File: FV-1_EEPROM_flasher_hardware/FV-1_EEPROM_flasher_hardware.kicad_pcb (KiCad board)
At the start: 2 copper layers, 64.9 x 84.9 mm, 20 parts, among them J1 TFT_SD, SW1 Up, SW2 Down, SW3 Right, SW4 Left, SW5 select, U1 24LC32, U2 24LC32

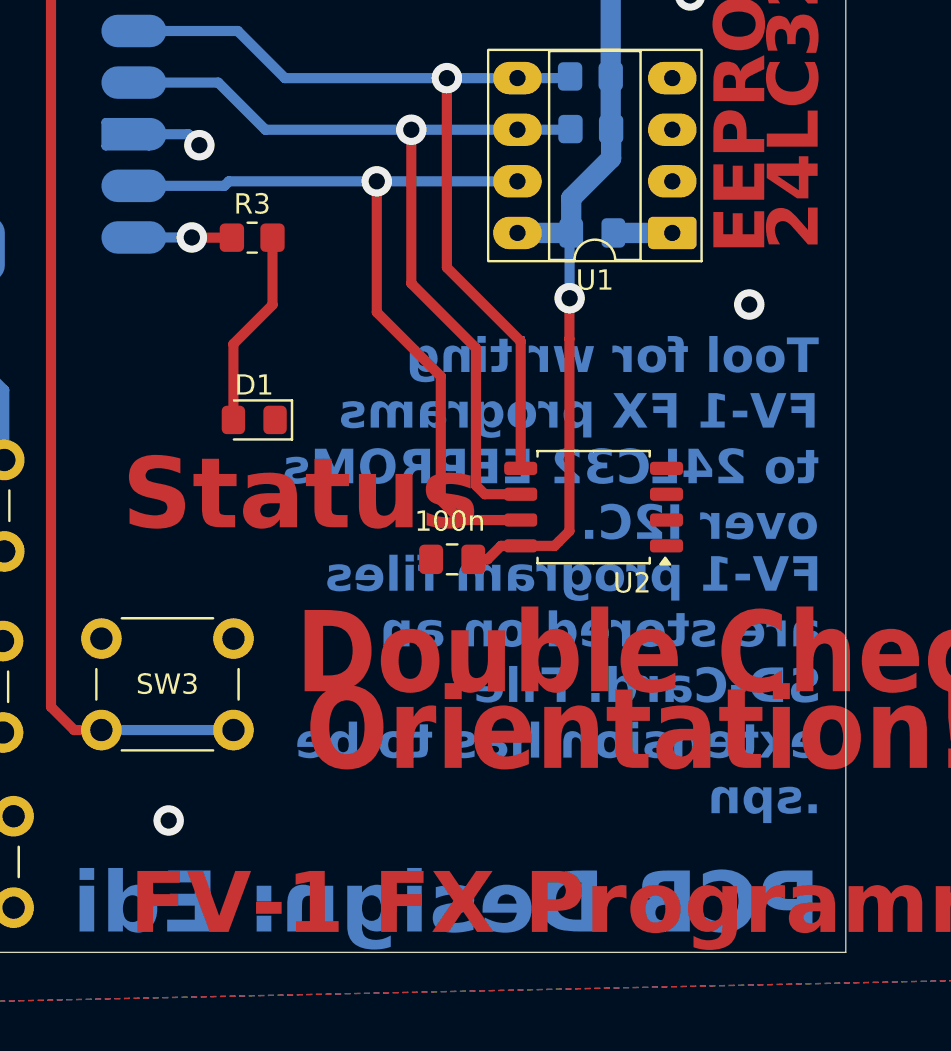
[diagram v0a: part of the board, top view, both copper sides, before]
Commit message: replaced status led with shift button, led connected to EEPROM write protect pin
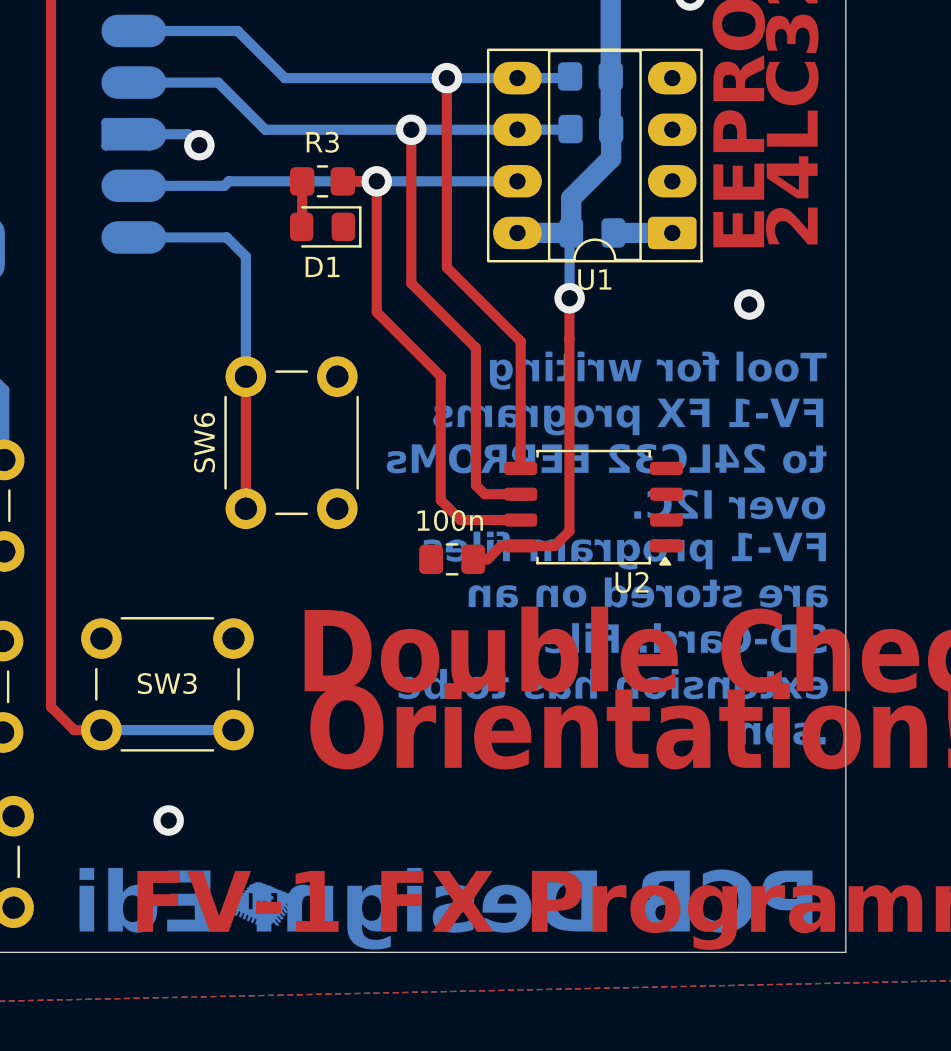
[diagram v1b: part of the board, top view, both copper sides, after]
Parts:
- added Ref**: Val**, Allgemein:PCB_EDI_logo, B.Cu at (180.0, 103.3)
- added SW6: select, Button_Switch_THT:SW_PUSH_6mm_H5mm, F.Cu at (179.2, 83.8)
- moved D1 10.1 mm to (182.9, 69.9)
- moved R3 4.43 mm to (182.9, 67.7), turned to 180 degrees
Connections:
- A1 pad 20: /Pgrm_Led -> /btn_shift
- J1 pad 9: /SD_SCK -> /SPI_SCK
- R3 pad 1: /Pgrm_Led -> /EEPROM_WP
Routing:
- net /btn_shift: track 0.00 -> 18.3 mm
- net Net-(D1-A): track 9.77 -> 2.25 mm
- net /Pgrm_Led: track 4.82 -> 0.00 mm, vias 1 -> 0
- net /EEPROM_WP: track 40.6 -> 42.3 mm
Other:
- board text removed: "Status"

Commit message: flipped EEPROM socket by 90°; PCB ready for production
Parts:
- moved U1 7.81 mm to (200.7, 62.4), turned to -90 degrees
- moved C1 5.93 mm to (200.7, 66.4), turned to -90 degrees
- moved R1 5.01 mm to (193.0, 66.5), turned to -90 degrees
- moved Ref** 4.52 mm to (180.3, 107.8)
- moved R2 1.43 mm to (195.6, 66.4), turned to -90 degrees
- moved SW5 0.32 mm to (167.5, 94.7)
- moved SW3 0.28 mm to (178.3, 94.7)
- moved SW1 0.23 mm to (167.5, 85.9)
- moved SW2 0.23 mm to (167.5, 103.4)
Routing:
- net /EEPROM_WP: track 42.3 -> 55.7 mm
- net /EEPROM_SCL: track 43.7 -> 55.0 mm
- net +3V3: track 148.4 -> 156.8 mm
- net /EEPROM_SDA: track 43.2 -> 47.5 mm
- net GND: track 35.3 -> 31.8 mm, vias 17 -> 15
- net /btn_down: track 90.3 -> 89.5 mm
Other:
- board size 64.9 x 84.9 mm -> 64.9 x 89.1 mm
- board text added: ">"
- board text added: "Shift"
